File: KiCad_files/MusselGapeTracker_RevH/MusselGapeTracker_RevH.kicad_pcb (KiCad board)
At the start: 2 copper layers, 72.5 x 57.8 mm, 83 parts, among them J1 AVR_SPI_PRG_6PTH, U1 ATMEGA328P, U2 DS3231M+TRL, U3 DS3231MZ

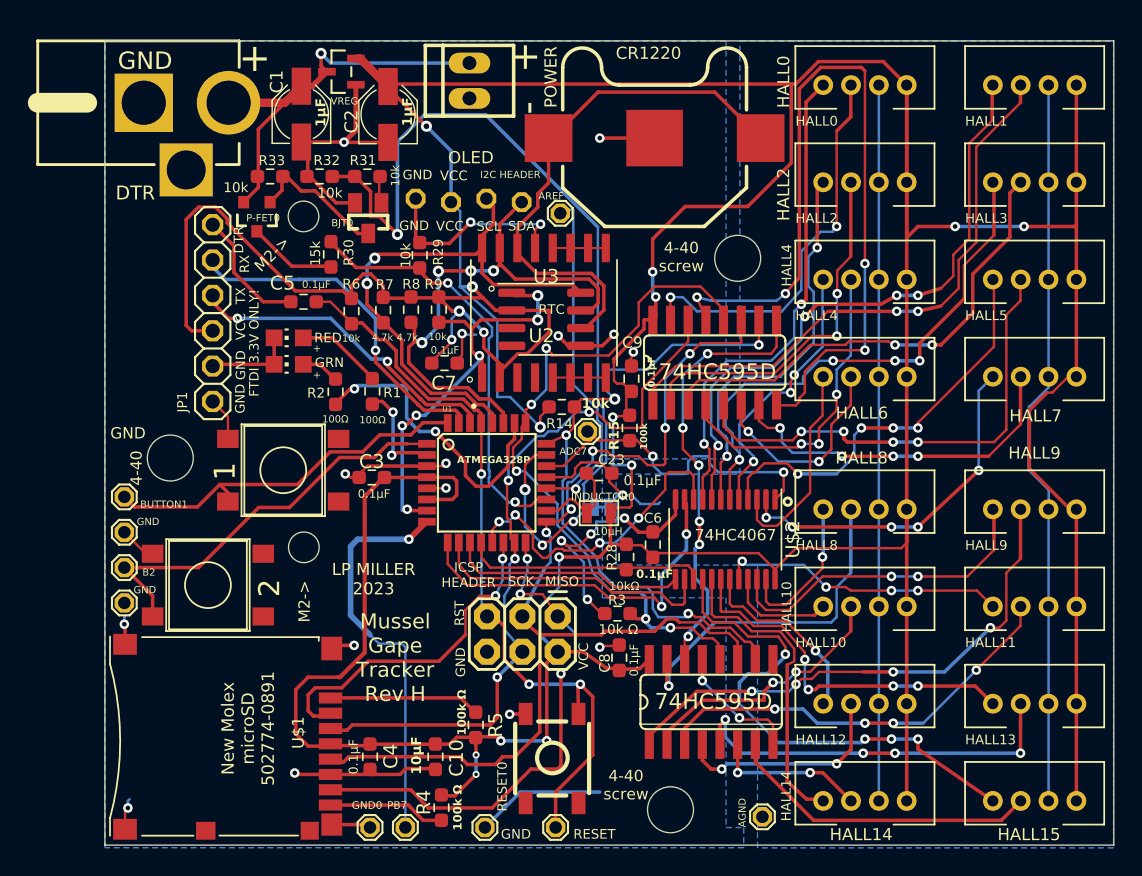
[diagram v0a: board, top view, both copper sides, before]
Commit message: replace Molex 502774-0891 with GCT MEM2052-00-195-00-A
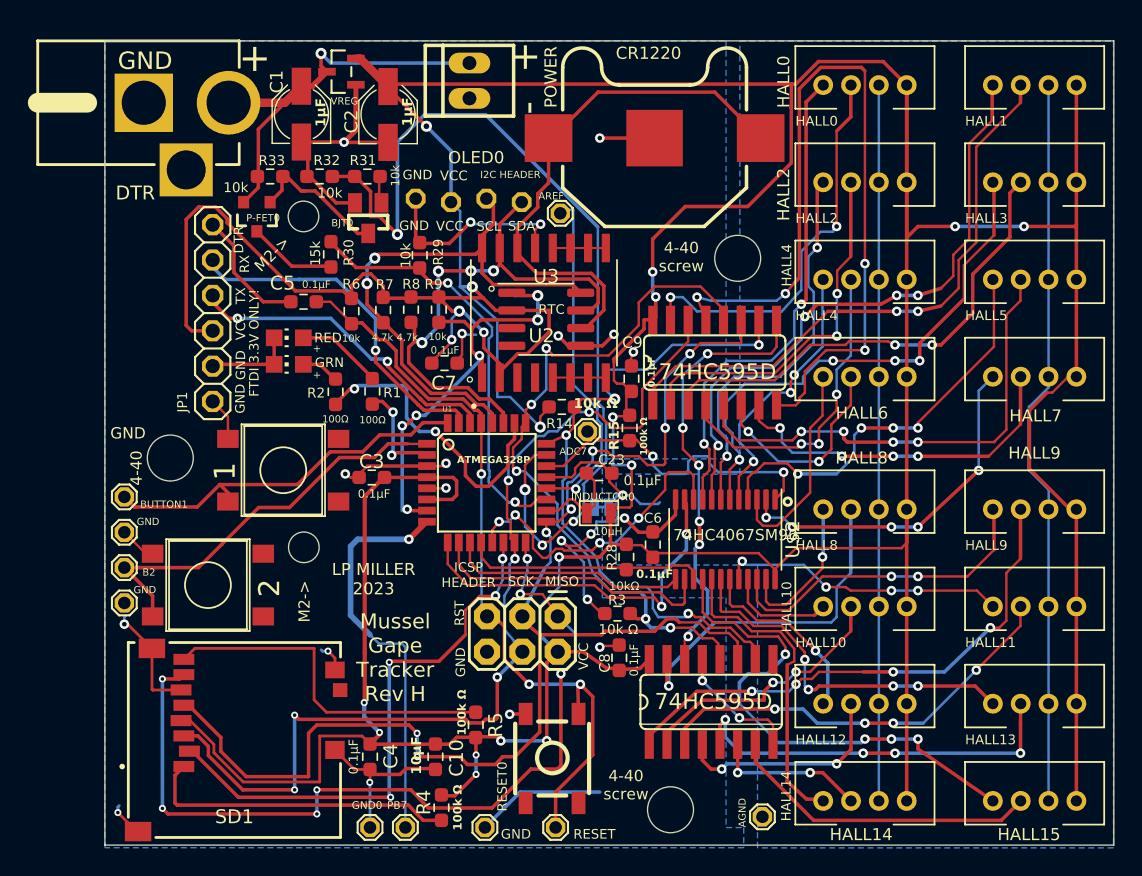
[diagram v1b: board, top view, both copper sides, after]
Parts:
- R14: value 10k -> 10k Ω
- R15: value 100k -> 100k Ω
- SD1: renamed from U$1; value MICROSD_MOLEX_REVERSECURRENT -> GCT_MEM2052-00-195-00-A_REVA; footprint MusselGapeTracker_RevE:MICROSD_SOCKET_MOLEX_REVERSEMOUNT -> MusselGapeTracker_RevH:GCT_MEM2052-00-195-00-A_REVA
- U$2: value 74HC4067 -> 74HC4067SM96
- moved SD1 8.44 mm to (107.3, 126.4), turned to -90 degrees
- renumbered OLED to OLED0
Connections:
- R4 pad 1: Net-(U$1-DAT2_RES) -> Net-(SD1-DAT2)
- R5 pad 1: Net-(U$1-DAT1_NC) -> Net-(SD1-DAT1)
- U2 pad 11: unconnected-(U2-N.C.-Pad10) -> unconnected-(U2-N.C.-Pad10)_4
- U2 pad 12: unconnected-(U2-N.C.-Pad10) -> unconnected-(U2-N.C.-Pad10)_7
- U2 pad 5: unconnected-(U2-N.C.-Pad10) -> unconnected-(U2-N.C.-Pad10)_5
- U2 pad 6: unconnected-(U2-N.C.-Pad10) -> unconnected-(U2-N.C.-Pad10)_1
- U2 pad 7: unconnected-(U2-N.C.-Pad10) -> unconnected-(U2-N.C.-Pad10)_3
- U2 pad 8: unconnected-(U2-N.C.-Pad10) -> unconnected-(U2-N.C.-Pad10)_2
- U2 pad 9: unconnected-(U2-N.C.-Pad10) -> unconnected-(U2-N.C.-Pad10)_6
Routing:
- net Net-(SD1-DAT1): track 0.00 -> 25.4 mm
- net /MISO: track 37.6 -> 62.6 mm, vias 3 -> 7
- net Net-(SD1-DAT2): track 0.00 -> 22.6 mm
- net /SCK: track 77.0 -> 95.2 mm, vias 5 -> 7
- net /MOSI: track 53.0 -> 70.8 mm, vias 4 -> 6
- net /CS_SD: track 24.5 -> 40.2 mm, vias 2 -> 4
- net VCC: track 419.7 -> 430.8 mm, vias 17 -> 19
- net Net-(U$1-DAT1_NC): track 10.9 -> 0.00 mm
- net Net-(U$1-DAT2_RES): track 8.47 -> 0.00 mm
- net GND: track 184.5 -> 191.0 mm
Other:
- board text removed: "New Molex microSD 502774-0891"

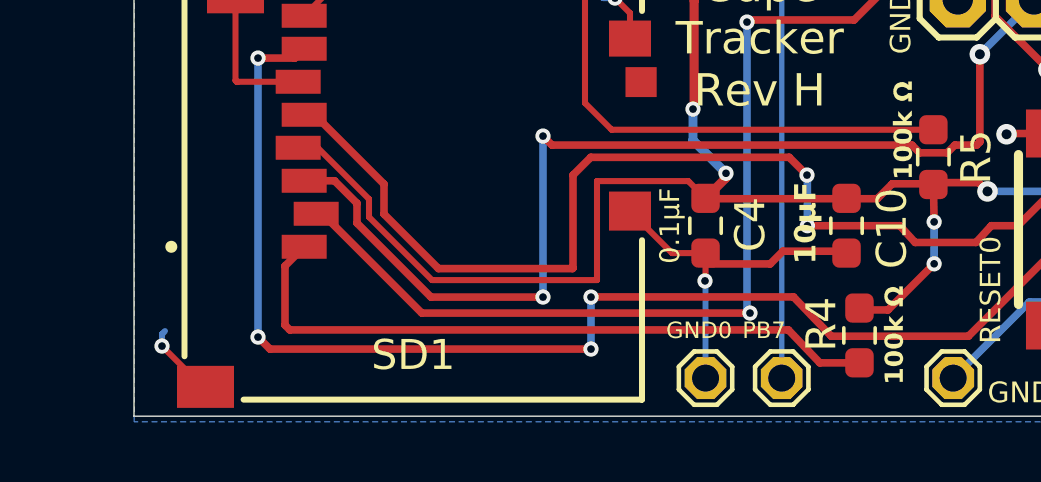
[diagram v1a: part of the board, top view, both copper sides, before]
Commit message: replace Molex 502774-0891 with GCT MEM2052-00-195-00-A
Pre-existing DRC errors (34) unrelated to this change.
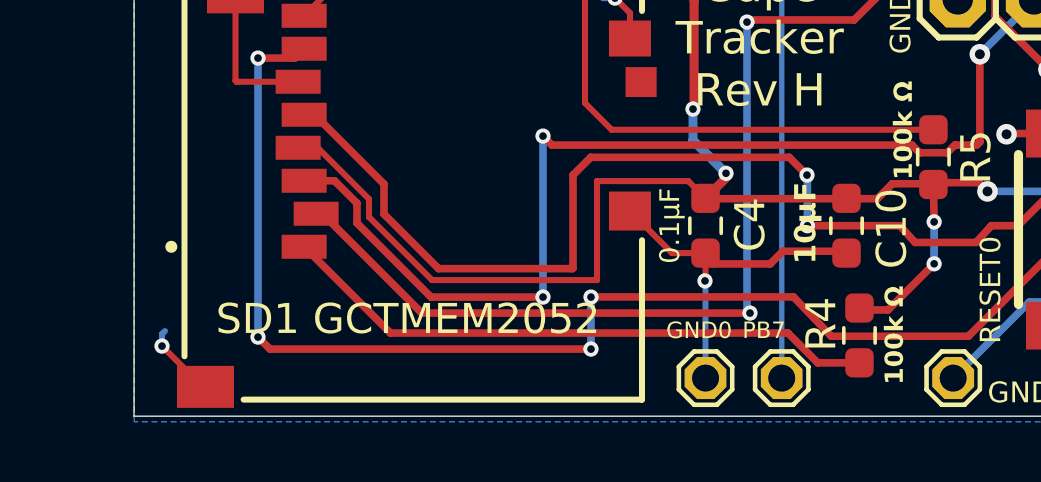
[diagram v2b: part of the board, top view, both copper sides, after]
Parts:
- SD1 GCTMEM2052: renamed from SD1
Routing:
- net Net-(SD1-DAT2): track 22.6 -> 20.1 mm
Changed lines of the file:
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@@
 		(layer "F.Cu")
 		(at 107.2874 126.3944 -90)
-		(property "Reference" "SD1"
-			(at 5.515 0 180)
+		(property "Reference" "SD1 GCTMEM2052"
+			(at 4.315 0.175 180)
 			(layer "F.SilkS")
 			(effects
@@
 	)
 	(segment
-		(start 119.7929 131.0707)
-		(end 103.1737 131.0707)
-		(width 0.254)
-		(layer "F.Cu")
-		(net 92)
-	)
-	(segment
-		(start 103.0124 128.9394)
-		(end 103.6524 128.2994)
-		(width 0.254)
+		(start 122.0969 132.1691)
+		(end 122.1613 132.1047)
+		(width 0.1778)
 		(layer "F.Cu")
 		(net 92)
 	)
 	(segment
-		(start 120.8405 132.1691)
-		(end 119.7929 131.0707)
+		(start 120.7721 132.1691)
+		(end 119.778 131.175)
 		(width 0.254)
 		(layer "F.Cu")
@@
 	)
 	(segment
-		(start 122.0969 132.1691)
-		(end 122.1613 132.1047)
-		(width 0.1778)
-		(layer "F.Cu")
-		(net 92)
-	)
-	(segment
-		(start 122.0969 132.1691)
-		(end 120.8405 132.1691)
+		(start 106.528 131.175)
+		(end 103.6524 128.2994)
 		(width 0.254)
 		(layer "F.Cu")
@@
 	)
 	(segment
-		(start 103.1737 131.0707)
-		(end 103.0124 130.9094)
+		(start 119.778 131.175)
+		(end 106.528 131.175)
 		(width 0.254)
 		(layer "F.Cu")
@@
 	)
 	(segment
-		(start 103.0124 130.9094)
-		(end 103.0124 128.9394)
+		(start 122.0969 132.1691)
+		(end 120.7721 132.1691)
 		(width 0.254)
 		(layer "F.Cu")

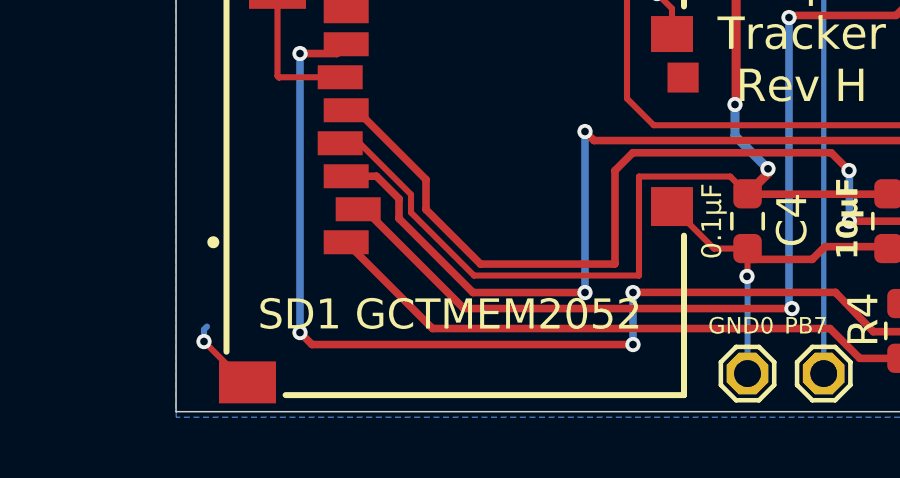
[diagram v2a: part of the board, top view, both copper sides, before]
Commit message: Update p-channel mosfet from BSH203 to SSM3J328R
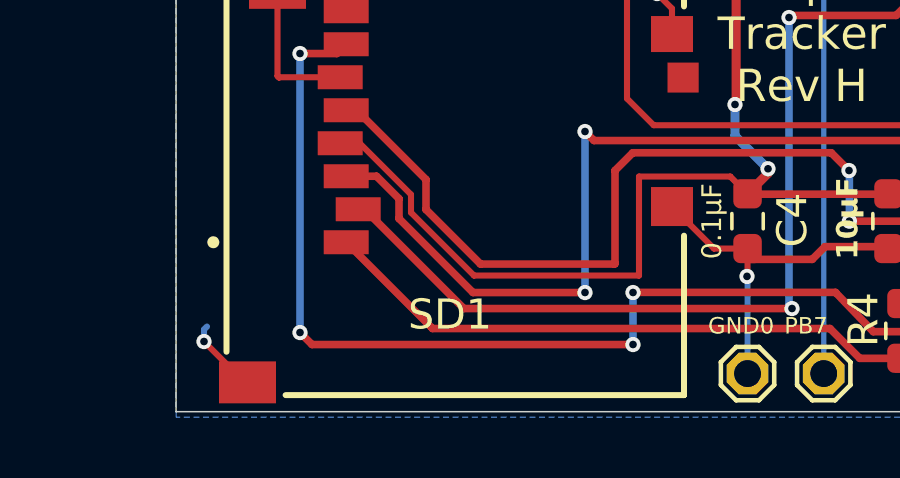
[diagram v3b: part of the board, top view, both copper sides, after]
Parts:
- SD1: renamed from SD1 GCTMEM2052
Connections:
- R30 pad 2: Net-(P-FET0-D) -> Net-(Q1-D)
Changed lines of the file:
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@@
 	(net 93 "Net-(SD1-DAT1)")
 	(net 94 "unconnected-(SD1-CD_PIN-PadCARD_DETECT9)")
+	(net 95 "Net-(Q1-D)")
 	(footprint "MusselGapeTracker_RevE:SOT95P237X112-3N"
 		(layer "F.Cu")
@@
 		(layer "F.Cu")
 		(at 107.2874 126.3944 -90)
-		(property "Reference" "SD1 GCTMEM2052"
+		(property "Reference" "SD1"
 			(at 4.315 0.175 180)
 			(layer "F.SilkS")
@@
 			(layers "F.Cu" "F.Mask" "F.Paste")
 			(roundrect_rratio 0.25)
-			(net 62 "Net-(P-FET0-D)")
+			(net 95 "Net-(Q1-D)")
 			(pinfunction "2")
 			(pintype "passive")
